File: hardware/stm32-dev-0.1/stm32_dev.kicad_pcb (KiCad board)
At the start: 2 copper layers, 46 parts, among them J1 USB_C_Receptacle_USB2.0, J2 SWD, J3 UART, J4 Spare, J5 Breakout, J6 Breakout, SW1 SIDE, SW2 SIDE, SW3 SW_Push, T1 Trackball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

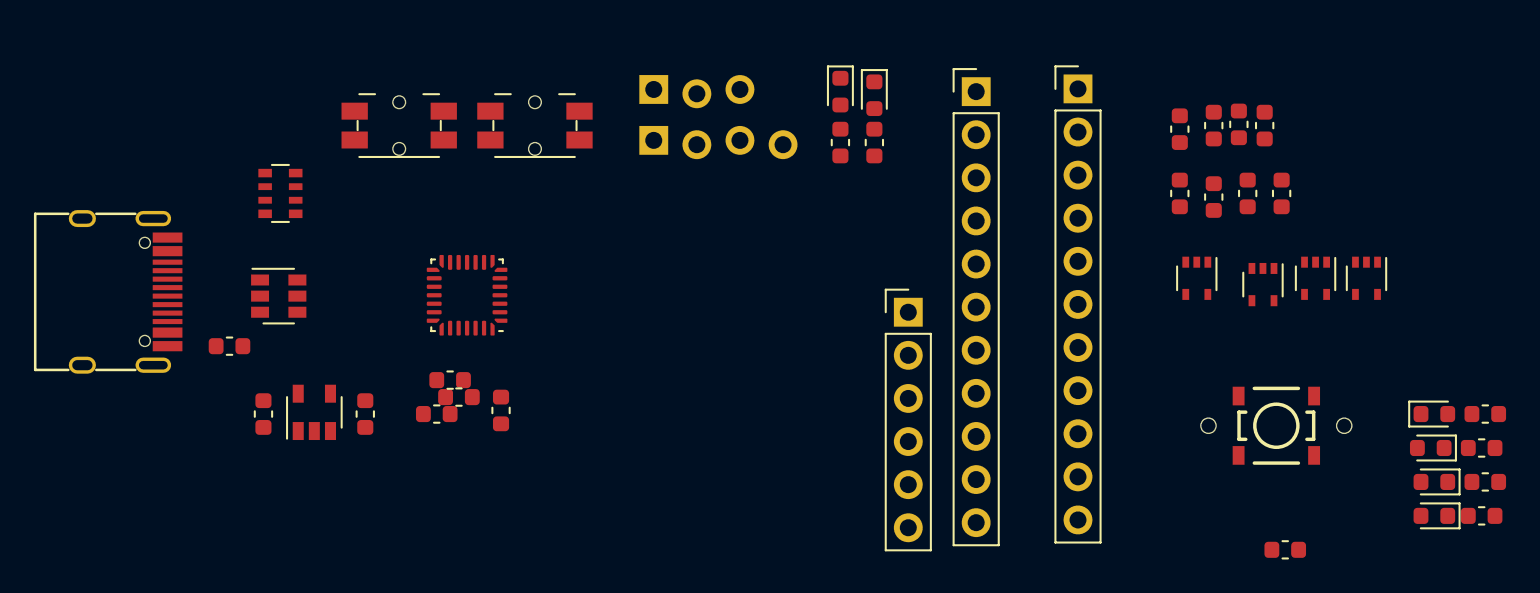
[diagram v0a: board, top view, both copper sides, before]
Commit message: Rough board layout (without routing yet), arrange components, add fiducials, pours, etc...
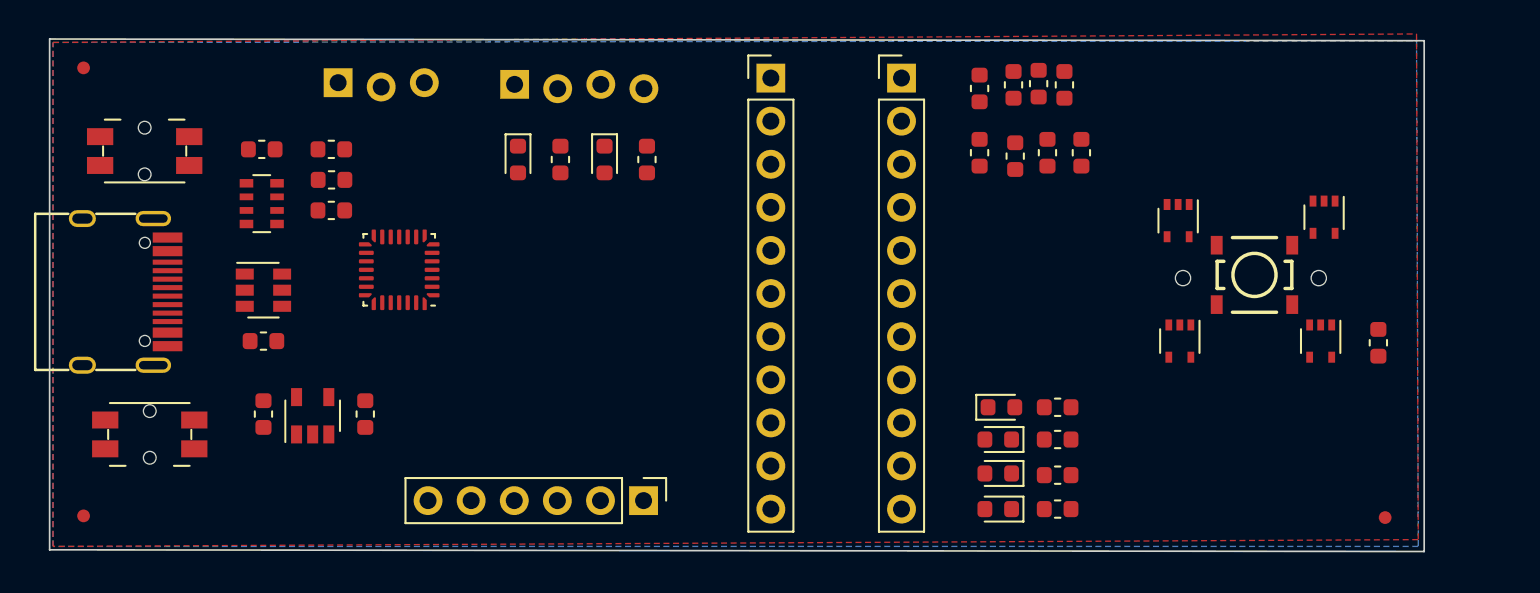
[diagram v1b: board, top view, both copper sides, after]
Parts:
- added FID1: Fiducial_0.75mm_Mask1.5mm, Fiducial:Fiducial_0.75mm_Mask1.5mm, F.Cu at (78.4, 114.0)
- added FID2: Fiducial_0.75mm_Mask1.5mm, Fiducial:Fiducial_0.75mm_Mask1.5mm, F.Cu at (78.4, 87.6)
- added FID3: Fiducial_0.75mm_Mask1.5mm, Fiducial:Fiducial_0.75mm_Mask1.5mm, F.Cu at (155.1, 114.1)
- moved SW2 29.1 mm to (82.3, 109.2), turned to 180 degrees
- moved D4 25.7 mm to (132.3, 111.5)
- moved D3 25.7 mm to (132.3, 113.6)
- moved D6 25.5 mm to (132.5, 107.6)
- moved D5 25.5 mm to (132.3, 109.5)
- moved R10 25.2 mm to (135.8, 107.6)
- moved R8 25.2 mm to (135.8, 111.6)
- moved R9 25.0 mm to (135.8, 109.5)
- moved R7 25.0 mm to (135.8, 113.6)
- moved C2 20.9 mm to (88.9, 92.4), turned to 180 degrees
- moved D1 19.4 mm to (104.0, 93.0)
- moved J4 19.1 mm to (111.4, 113.1), turned to 270 degrees
- moved J3 18.6 mm to (93.4, 88.6)
- moved R1 16.5 mm to (106.5, 93.0), turned to 90 degrees
- moved D2 16.3 mm to (109.1, 93.0)
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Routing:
- added copper zone on F.Cu, net +3V3
- added copper zone on B.Cu, net GND
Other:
- board outline added: 81 x 30.2 mm
